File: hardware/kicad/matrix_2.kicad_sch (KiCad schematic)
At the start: 166 parts, among them U6 IS31FL3741A

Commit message: Update KiCAD files
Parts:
- removed R64, R65: 4.7k, Resistor_SMD:R_0402_1005Metric, symbol Device:R_Small_US

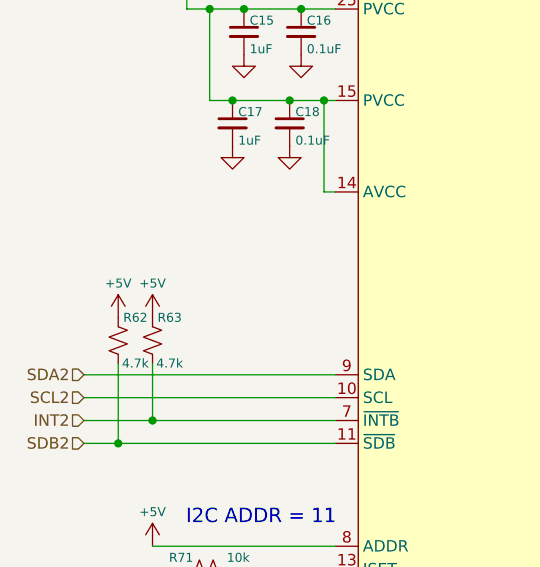
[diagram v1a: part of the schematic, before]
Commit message: Update KiCAD files
correct files this time :)
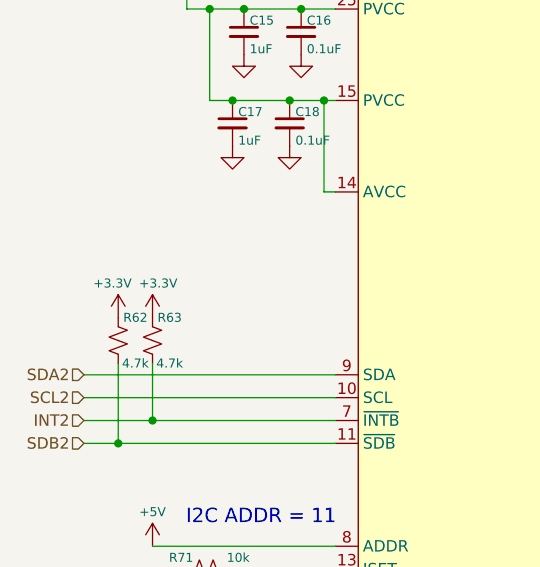
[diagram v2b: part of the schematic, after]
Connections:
- net +5V: no longer R62.1, R63.1
- new net +3.3V: R62.1, R63.1
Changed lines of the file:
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@@
 	)
 	(symbol
+		(lib_id "power:+3.3V")
+		(at 36.83 72.39 0)
+		(unit 1)
+		(exclude_from_sim no)
+		(in_bom yes)
+		(on_board yes)
+		(dnp no)
+		(property "Reference" "#PWR055"
+			(at 36.83 76.2 0)
+			(effects
+				(font
+					(size 1.27 1.27)
+				)
+				(hide yes)
+			)
+		)
+		(property "Value" "+3.3V"
+			(at 36.195 68.58 0)
+			(effects
+				(font
+					(size 1 1)
+				)
+			)
+		)
+		(property "Footprint" ""
+			(at 36.83 72.39 0)
+			(effects
+				(font
+					(size 1.27 1.27)
+				)
+				(hide yes)
+			)
+		)
+		(property "Datasheet" ""
+			(at 36.83 72.39 0)
+			(effects
+				(font
+					(size 1.27 1.27)
+				)
+				(hide yes)
+			)
+		)
+		(property "Description" "Power symbol creates a global label with name \"+3.3V\""
+			(at 36.83 72.39 0)
+			(effects
+				(font
+					(size 1.27 1.27)
+				)
+				(hide yes)
+			)
+		)
+		(pin "1"
+		)
+		(instances
+			(project "traffic_paradise"
+				(path "/911505fc-874d-4338-908e-12054bdd5112/a4b8a9ee-0dc2-43fe-8aa1-46a166ad2321"
+					(reference "#PWR055")
+					(unit 1)
+				)
+			)
+		)
+	)
+	(symbol
 		(lib_id "Device:R_Small_US")
 		(at 137.16 194.31 90)
@@
 	)
 	(symbol
+		(lib_id "power:+3.3V")
+		(at 40.64 72.39 0)
+		(unit 1)
+		(exclude_from_sim no)
+		(in_bom yes)
+		(on_board yes)
+		(dnp no)
+		(property "Reference" "#PWR057"
+			(at 40.64 76.2 0)
+			(effects
+				(font
+					(size 1.27 1.27)
+				)
+				(hide yes)
+			)
+		)
+		(property "Value" "+3.3V"
+			(at 41.275 68.58 0)
+			(effects
+				(font
+					(size 1 1)
+				)
+			)
+		)
+		(property "Footprint" ""
+			(at 40.64 72.39 0)
+			(effects
+				(font
+					(size 1.27 1.27)
+				)
+				(hide yes)
+			)
+		)
+		(property "Datasheet" ""
+			(at 40.64 72.39 0)
+			(effects
+				(font
+					(size 1.27 1.27)
+				)
+				(hide yes)
+			)
+		)
+		(property "Description" "Power symbol creates a global label with name \"+3.3V\""
+			(at 40.64 72.39 0)
+			(effects
+				(font
+					(size 1.27 1.27)
+				)
+				(hide yes)
+			)
+		)
+		(pin "1"
+		)
+		(instances
+			(project "traffic_paradise"
+				(path "/911505fc-874d-4338-908e-12054bdd5112/a4b8a9ee-0dc2-43fe-8aa1-46a166ad2321"
+					(reference "#PWR057")
+					(unit 1)
+				)
+			)
+		)
+	)
+	(symbol
 		(lib_id "Device:LED_RABG")
 		(at 215.9 226.06 0)
@@
 	)
 	(symbol
-		(lib_id "power:+5V")
-		(at 40.64 72.39 0)
-		(unit 1)
-		(exclude_from_sim no)
-		(in_bom yes)
-		(on_board yes)
-		(dnp no)
-		(property "Reference" "#PWR062"
-			(at 40.64 76.2 0)
-			(effects
-				(font
-					(size 1.27 1.27)
-				)
-				(hide yes)
-			)
-		)
-		(property "Value" "+5V"
-			(at 40.64 68.58 0)
-			(effects
-				(font
-					(size 1 1)
-				)
-			)
-		)
-		(property "Footprint" ""
-			(at 40.64 72.39 0)
-			(effects
-				(font
-					(size 1.27 1.27)
-				)
-				(hide yes)
-			)
-		)
-		(property "Datasheet" ""
-			(at 40.64 72.39 0)
-			(effects
-				(font
-					(size 1.27 1.27)
-				)
-				(hide yes)
-			)
-		)
-		(property "Description" "Power symbol creates a global label with name \"+5V\""
-			(at 40.64 72.39 0)
-			(effects
-				(font
-					(size 1.27 1.27)
-				)
-				(hide yes)
-			)
-		)
-		(pin "1"
-		)
-		(instances
-			(project "v0"
-				(path "/911505fc-874d-4338-908e-12054bdd5112/a4b8a9ee-0dc2-43fe-8aa1-46a166ad2321"
-					(reference "#PWR062")
-					(unit 1)
-				)
-			)
-		)
-	)
-	(symbol
 		(lib_id "Device:R_Small_US")
 		(at 137.16 213.36 90)
@@
 					(unit 1)
 				)
-			)
-		)
-	)
-	(symbol
-		(lib_id "power:+5V")
-		(at 36.83 72.39 0)
-		(unit 1)
-		(exclude_from_sim no)
-		(in_bom yes)
-		(on_board yes)
-		(dnp no)
-		(property "Reference" "#PWR061"
-			(at 36.83 76.2 0)
-			(effects
-				(font
-					(size 1.27 1.27)
-				)
-				(hide yes)
-			)
-		)
-		(property "Value" "+5V"
-			(at 36.83 68.58 0)
-			(effects
-				(font
-					(size 1 1)
-				)
-			)
-		)
-		(property "Footprint" ""
-			(at 36.83 72.39 0)
-			(effects
-				(font
-					(size 1.27 1.27)
-				)
-				(hide yes)
-			)
-		)
-		(property "Datasheet" ""
-			(at 36.83 72.39 0)
-			(effects
-				(font
-					(size 1.27 1.27)
-				)
-				(hide yes)
-			)
-		)
-		(property "Description" "Power symbol creates a global label with name \"+5V\""
-			(at 36.83 72.39 0)
-			(effects
-				(font
-					(size 1.27 1.27)
-				)
-				(hide yes)
-			)
-		)
-		(pin "1"
-		)
-		(instances
-			(project "v0"
-				(path "/911505fc-874d-4338-908e-12054bdd5112/a4b8a9ee-0dc2-43fe-8aa1-46a166ad2321"
-					(reference "#PWR061")
-					(unit 1)
-				)

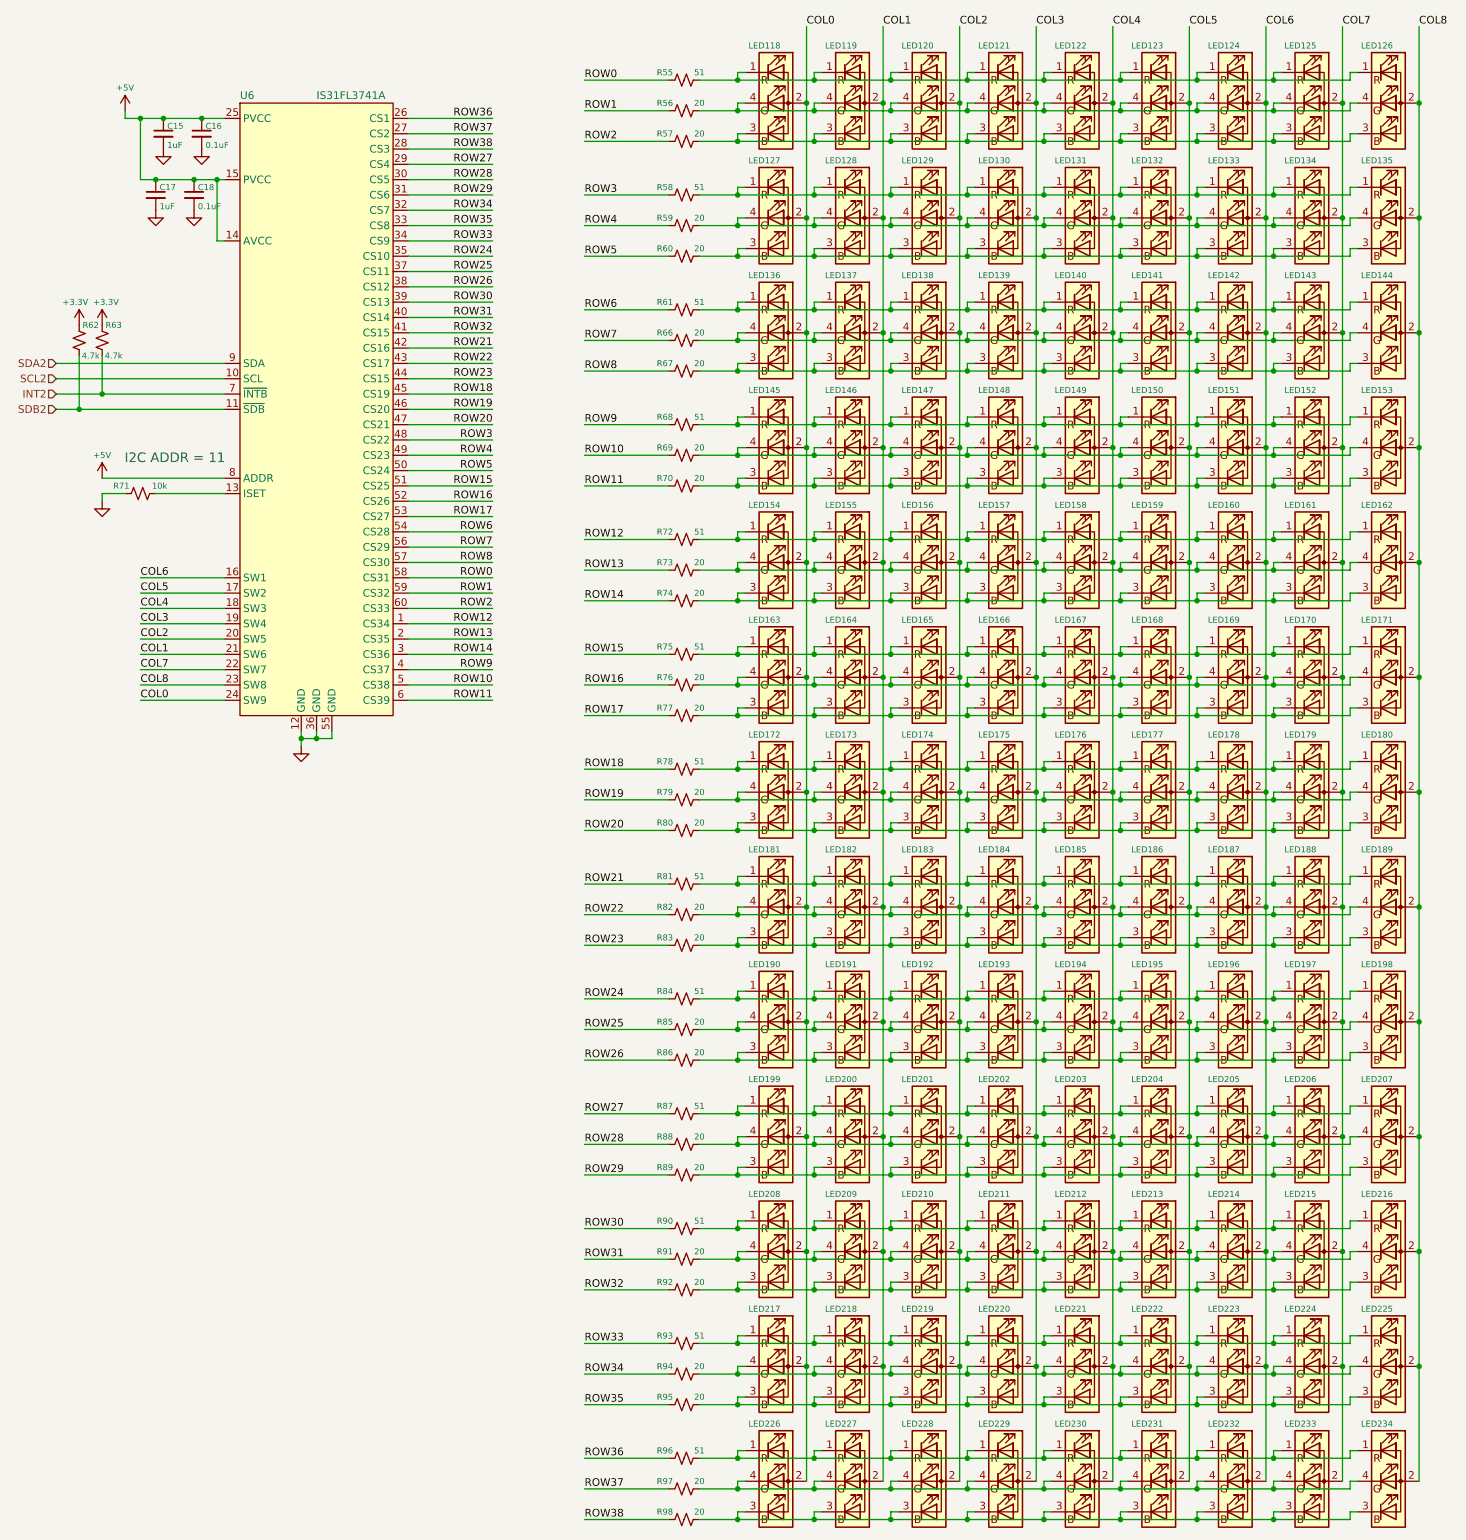
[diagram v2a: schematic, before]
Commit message: add and route matrix 4
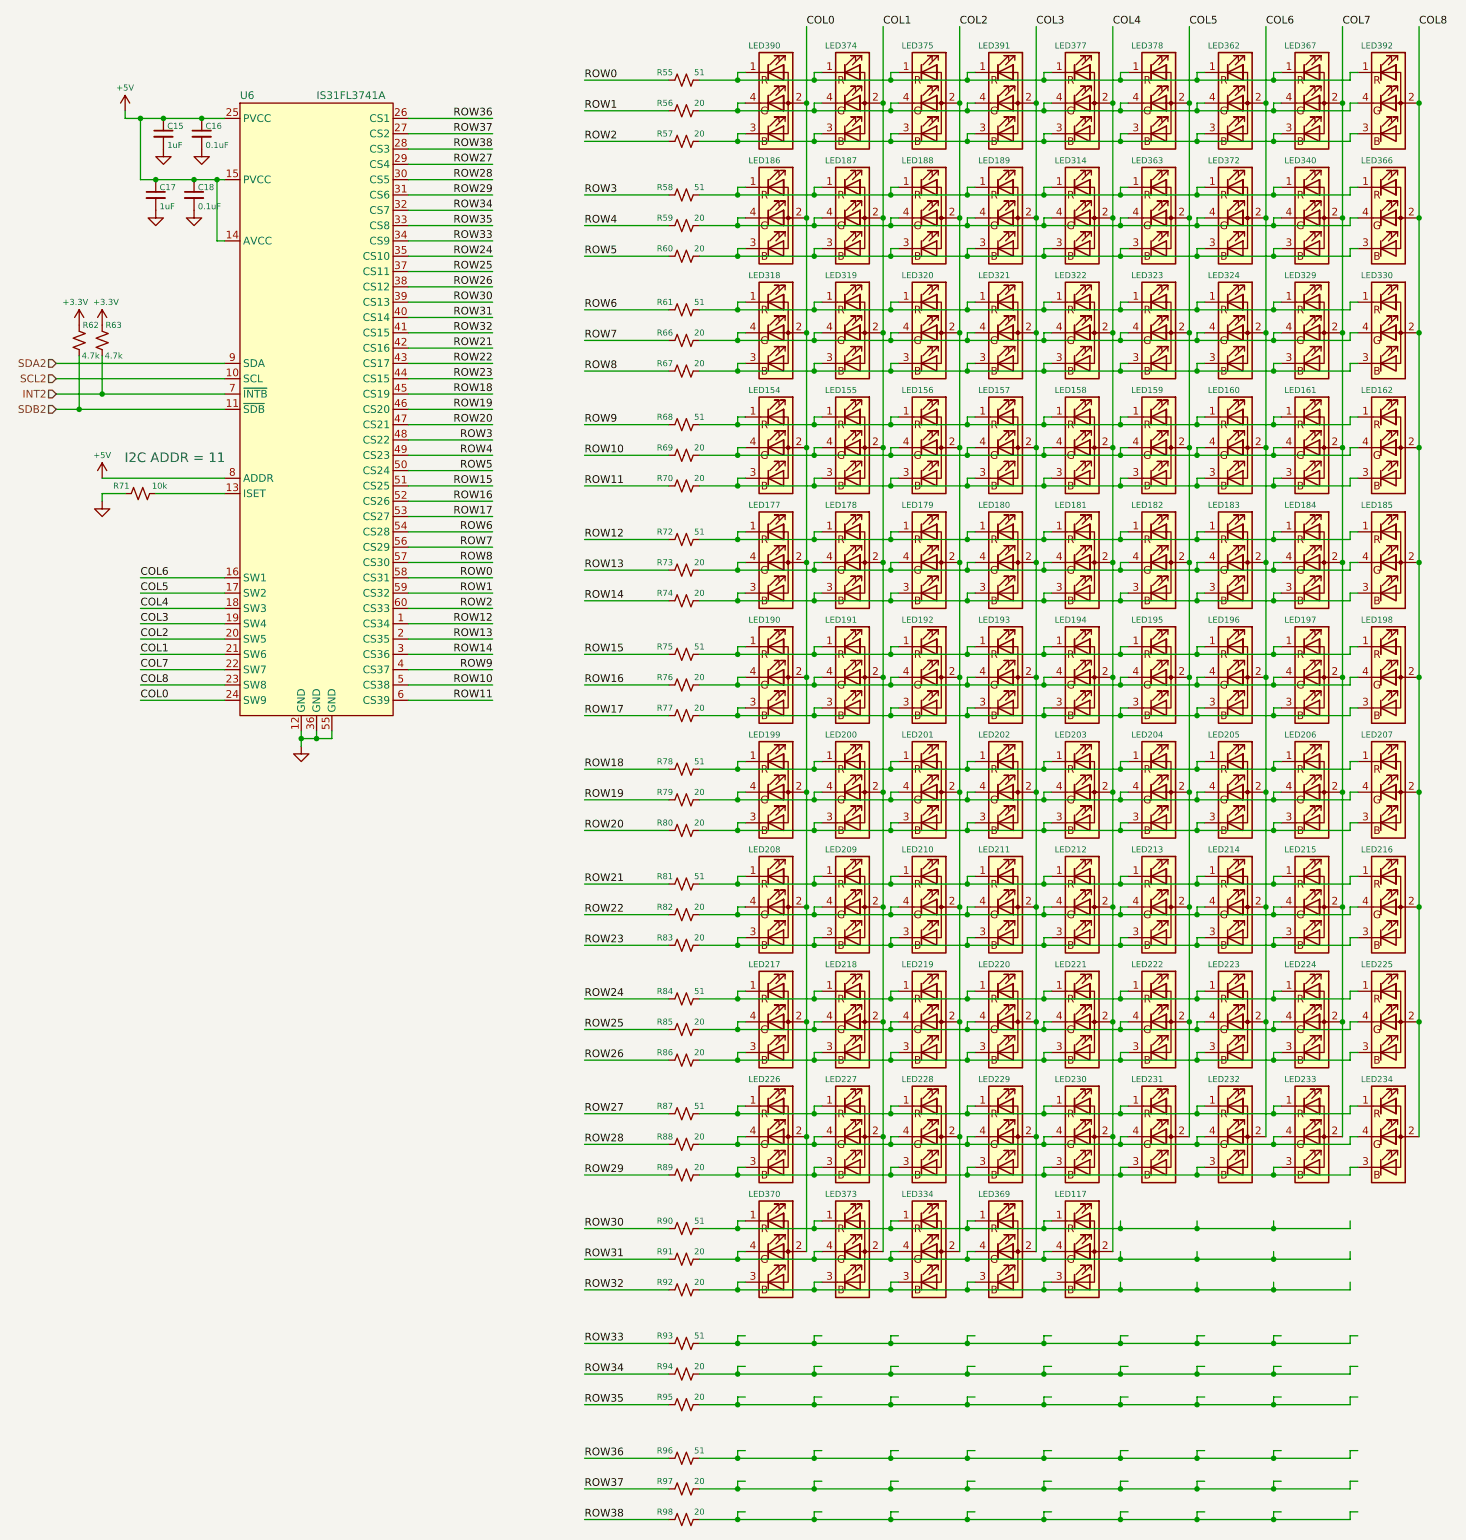
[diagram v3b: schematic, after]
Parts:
- removed LED118, LED119, LED120, LED121, LED122, LED123, LED124, LED125, LED126, LED127, LED128, LED129, LED130, LED131, LED132, LED133, LED134, LED135, LED136, LED137, LED138, LED139, LED140, LED141, LED142, LED143, LED144, LED145, LED146, LED147, LED148, LED149, LED150, LED151, LED152, LED153, LED163, LED164, LED165, LED166, LED167, LED168, LED169, LED170, LED171, LED172, LED173, LED174, LED175, LED176: LED_ARGB, map_lbr:LED_RGB_0606, symbol Device:LED_RABG
- added LED117, LED314, LED318, LED319, LED320, LED321, LED322, LED323, LED324, LED329, LED330, LED334, LED340, LED362, LED363, LED366, LED367, LED369, LED370, LED372, LED373, LED374, LED375, LED377, LED378, LED390, LED391, LED392: LED_ARGB, map_lbr:LED_RGB_0606, symbol Device:LED_RABG
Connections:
- net COL0: now also LED177.2 (A), LED186.2 (A), LED318.2 (A), LED370.2 (A), LED390.2 (A); no longer LED181.2 (A)
- net COL1: now also LED178.2 (A), LED187.2 (A), LED319.2 (A), LED373.2 (A), LED374.2 (A); no longer LED182.2 (A)
- net COL2: now also LED179.2 (A), LED188.2 (A), LED320.2 (A), LED334.2 (A), LED375.2 (A); no longer LED183.2 (A)
- net COL3: now also LED180.2 (A), LED189.2 (A), LED321.2 (A), LED369.2 (A), LED391.2 (A); no longer LED184.2 (A)
- net COL4: now also LED181.2 (A), LED117.2 (A), LED314.2 (A), LED322.2 (A), LED377.2 (A); no longer LED185.2 (A)
- net COL5: now also LED182.2 (A), LED323.2 (A), LED363.2 (A), LED378.2 (A); no longer LED177.2 (A), LED186.2 (A)
- net COL6: now also LED183.2 (A), LED324.2 (A), LED362.2 (A), LED372.2 (A); no longer LED178.2 (A), LED187.2 (A)
- net COL7: now also LED184.2 (A), LED329.2 (A), LED340.2 (A), LED367.2 (A); no longer LED179.2 (A), LED188.2 (A)
- net COL8: now also LED185.2 (A), LED330.2 (A), LED366.2 (A), LED392.2 (A); no longer LED180.2 (A), LED189.2 (A)
- net at R75.2: now also LED190.1 (RK), LED191.1 (RK), LED192.1 (RK), LED193.1 (RK), LED194.1 (RK), LED195.1 (RK), LED196.1 (RK), LED197.1 (RK), LED198.1 (RK)
- net at R77.2: now also LED190.3 (BK), LED191.3 (BK), LED192.3 (BK), LED193.3 (BK), LED194.3 (BK), LED195.3 (BK), LED196.3 (BK), LED197.3 (BK), LED198.3 (BK)
- net at R76.2: now also LED190.4 (GK), LED191.4 (GK), LED192.4 (GK), LED193.4 (GK), LED194.4 (GK), LED195.4 (GK), LED196.4 (GK), LED197.4 (GK), LED198.4 (GK)
- net at LED181.1 (RK), LED182.1 (RK), LED183.1 (RK)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: now also LED177.1 (RK), LED178.1 (RK), LED179.1 (RK), LED180.1 (RK), R72.2; no longer LED186.1 (RK), LED187.1 (RK), LED188.1 (RK), LED189.1 (RK), R81.2
- net at LED181.3 (BK), LED182.3 (BK), LED183.3 (BK)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: now also LED177.3 (BK), LED178.3 (BK), LED179.3 (BK), LED180.3 (BK), R74.2; no longer LED186.3 (BK), LED187.3 (BK), LED188.3 (BK), LED189.3 (BK), R83.2
- net at LED181.4 (GK), LED182.4 (GK), LED183.4 (GK)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: now also LED177.4 (GK), LED178.4 (GK), LED179.4 (GK), LED180.4 (GK), R73.2; no longer LED186.4 (GK), LED187.4 (GK), LED188.4 (GK), LED189.4 (GK), R82.2
- net at R70.2: now also LED154.3 (BK), LED155.3 (BK), LED156.3 (BK), LED157.3 (BK), LED158.3 (BK), LED159.3 (BK), LED160.3 (BK), LED161.3 (BK), LED162.3 (BK)
- net at LED199.1 (RK), LED200.1 (RK), LED201.1 (RK)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: now also R78.2; no longer R87.2
- net at LED199.3 (BK), LED200.3 (BK), LED201.3 (BK)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: now also R80.2; no longer R89.2
- net at LED199.4 (GK), LED200.4 (GK), LED201.4 (GK)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: now also R79.2; no longer R88.2
- net at LED208.1 (RK), LED209.1 (RK), LED210.1 (RK)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: now also R81.2; no longer R90.2
- net at LED208.3 (BK), LED209.3 (BK), LED210.3 (BK)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: now also R83.2; no longer R92.2
- net at LED208.4 (GK), LED209.4 (GK), LED210.4 (GK)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: now also R82.2; no longer R91.2
- net at LED217.1 (RK), LED218.1 (RK), LED219.1 (RK)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: now also R84.2; no longer R93.2
- net at LED226.1 (RK), LED227.1 (RK), LED228.1 (RK)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: now also R87.2; no longer R96.2
- net at LED226.3 (BK), LED227.3 (BK), LED228.3 (BK)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: now also R89.2; no longer R98.2
- net at LED226.4 (GK), LED227.4 (GK), LED228.4 (GK)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: now also R88.2; no longer R97.2
- net at R59.2: now also LED186.4 (GK), LED187.4 (GK), LED188.4 (GK), LED189.4 (GK), LED314.4 (GK), LED340.4 (GK), LED363.4 (GK), LED366.4 (GK), LED372.4 (GK)
- net at R55.2: now also LED362.1 (RK), LED367.1 (RK), LED374.1 (RK), LED375.1 (RK), LED377.1 (RK), LED378.1 (RK), LED390.1 (RK), LED391.1 (RK), LED392.1 (RK)
- net at R57.2: now also LED362.3 (BK), LED367.3 (BK), LED374.3 (BK), LED375.3 (BK), LED377.3 (BK), LED378.3 (BK), LED390.3 (BK), LED391.3 (BK), LED392.3 (BK)
- net at R56.2: now also LED362.4 (GK), LED367.4 (GK), LED374.4 (GK), LED375.4 (GK), LED377.4 (GK), LED378.4 (GK), LED390.4 (GK), LED391.4 (GK), LED392.4 (GK)
- net at LED154.1 (RK), LED155.1 (RK), LED156.1 (RK)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: now also R68.2; no longer R72.2
- net at LED154.4 (GK), LED155.4 (GK), LED156.4 (GK)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: now also R69.2; no longer R73.2
- net at LED217.3 (BK), LED218.3 (BK), LED219.3 (BK)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: now also R86.2; no longer R95.2
- net at LED217.4 (GK), LED218.4 (GK), LED219.4 (GK)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: now also R85.2; no longer R94.2
- net at R61.2: now also LED318.1 (RK), LED319.1 (RK), LED320.1 (RK), LED321.1 (RK), LED322.1 (RK), LED323.1 (RK), LED324.1 (RK), LED329.1 (RK), LED330.1 (RK)
- net at R67.2: now also LED318.3 (BK), LED319.3 (BK), LED320.3 (BK), LED321.3 (BK), LED322.3 (BK), LED323.3 (BK), LED324.3 (BK), LED329.3 (BK), LED330.3 (BK)
- net at R66.2: now also LED318.4 (GK), LED319.4 (GK), LED320.4 (GK), LED321.4 (GK), LED322.4 (GK), LED323.4 (GK), LED324.4 (GK), LED329.4 (GK), LED330.4 (GK)
- net at R58.2: now also LED186.1 (RK), LED187.1 (RK), LED188.1 (RK), LED189.1 (RK), LED314.1 (RK), LED340.1 (RK), LED363.1 (RK), LED366.1 (RK), LED372.1 (RK)
- net at R60.2: now also LED186.3 (BK), LED187.3 (BK), LED188.3 (BK), LED189.3 (BK), LED314.3 (BK), LED340.3 (BK), LED363.3 (BK), LED366.3 (BK), LED372.3 (BK)
- new net: LED117.1 (RK), LED334.1 (RK), LED369.1 (RK), LED370.1 (RK), LED373.1 (RK), R90.2
- new net: LED117.3 (BK), LED334.3 (BK), LED369.3 (BK), LED370.3 (BK), LED373.3 (BK), R92.2
- new net: LED117.4 (GK), LED334.4 (GK), LED369.4 (GK), LED370.4 (GK), LED373.4 (GK), R91.2
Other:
- moved on the sheet: LED154, LED155, LED156, LED157, LED158, LED159, LED160, LED161, LED162, LED177, LED178, LED179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
